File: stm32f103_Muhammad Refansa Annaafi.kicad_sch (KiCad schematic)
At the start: 28 parts, among them J1 Conn_01x04_Pin, J2 USB_B_Micro, J3 Conn_01x06_Pin, J4 Conn_01x04_Pin, SW2 SW_SPDT, U1 STM32F100C8Tx, U2 AMS1117, Y1 Crystal 16 Mhz

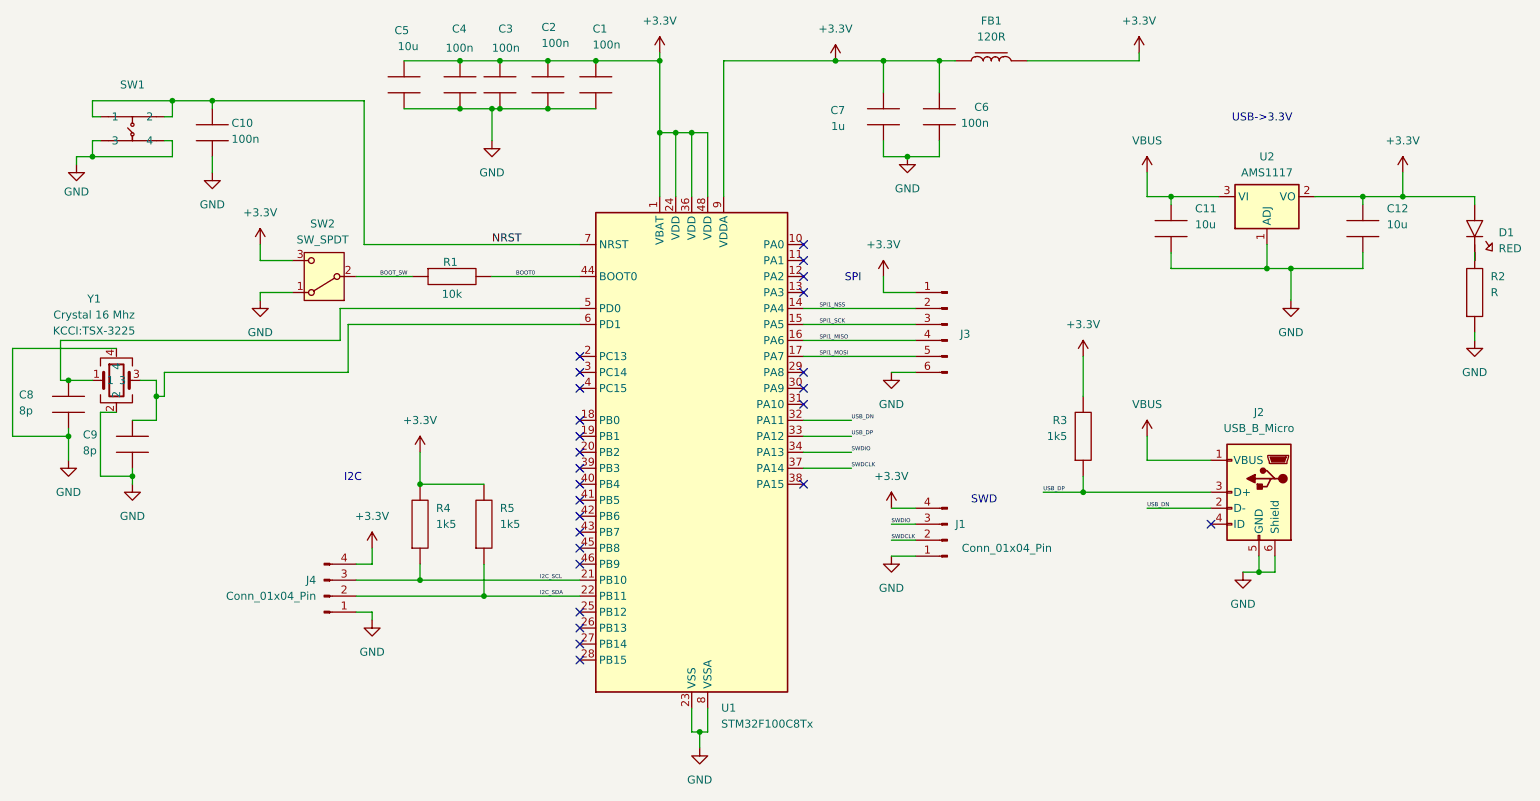
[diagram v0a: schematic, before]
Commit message: Rename MCU to STM32F103 and set R2 to 1k
Update schematic, BOM, README, and schematic screenshot.
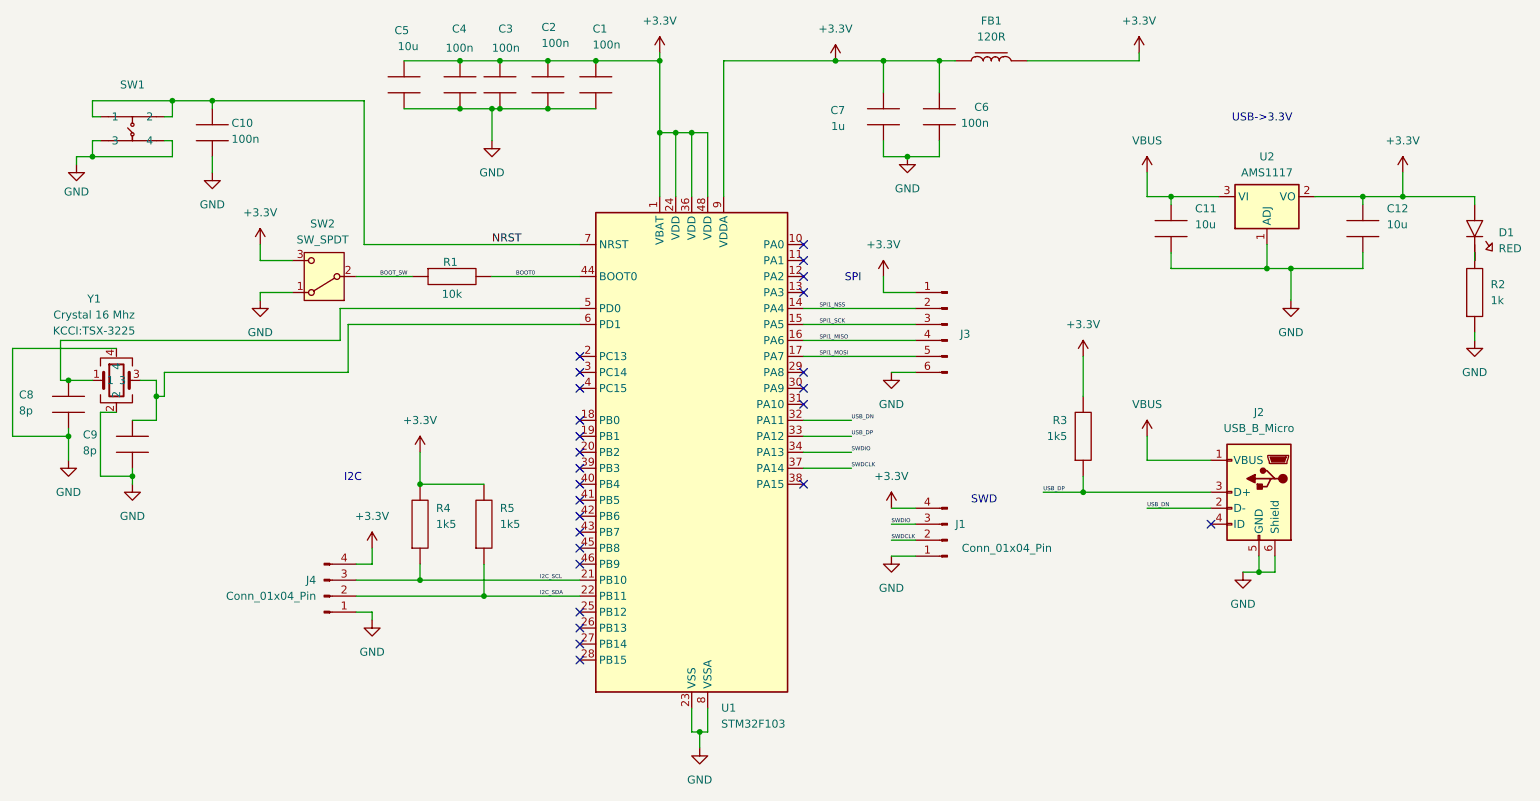
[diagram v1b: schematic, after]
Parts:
- R2: value R -> 1k
- U1: value STM32F100C8Tx -> STM32F103
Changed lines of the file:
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@@
 		(fields_autoplaced yes)
 		(property "Reference" "R2"
-			(at 255.27 76.1999 90)
-			(effects
-				(font
-					(size 1.27 1.27)
-				)
-				(justify right)
-			)
-		)
-		(property "Value" "R"
-			(at 255.27 78.7399 90)
+			(at 255.27 77.4699 90)
+			(effects
+				(font
+					(size 1.27 1.27)
+				)
+				(justify right)
+			)
+		)
+		(property "Value" "1k"
+			(at 255.27 80.0099 90)
 			(effects
 				(font
@@
 			)
 		)
-		(property "Value" "STM32F100C8Tx"
+		(property "Value" "STM32F103"
 			(at 132.9533 147.32 0)
 			(effects
